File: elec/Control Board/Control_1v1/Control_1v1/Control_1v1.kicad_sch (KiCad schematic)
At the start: 69 parts, among them J1 DB9_Female_MountingHoles, J10 Conn_02x12_Odd_Even, J11 Screw_Terminal_01x02, J14 Conn_01x10, J2 Conn_01x08, J25 Screw_Terminal_01x02, J3 Conn_01x08, J4 Conn_01x08, J5 Conn_01x08, J6 Conn_01x08, J7 Conn_01x10, J8 Conn_02x18_Odd_Even, J9 Conn_01x10

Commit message: Add sheet with title block.
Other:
- moved on the sheet: A1, C104, C301, H1, H2, H3, H4, H5, ISO1, ISO2, ISO3, ISO4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

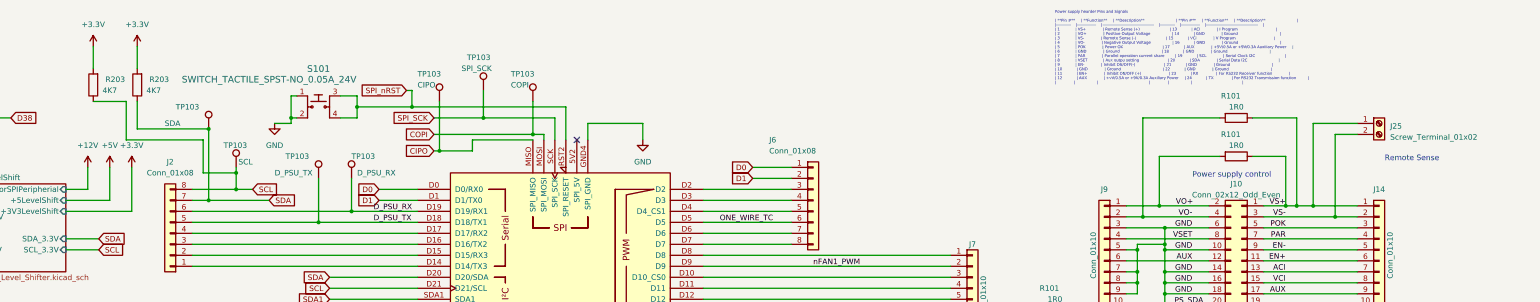
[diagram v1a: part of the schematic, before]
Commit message: Fix J10 backwards.
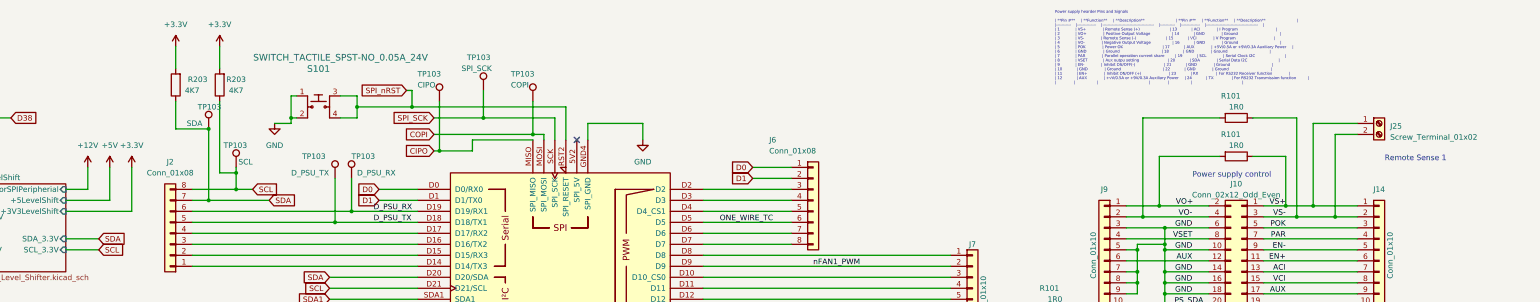
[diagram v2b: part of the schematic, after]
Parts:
- J10: footprint Connector_PinHeader_2.00mm:PinHeader_2x12_P2.00mm_Vertical -> PubInv_KiCad_PCB.pretty:PinHeader_2x12_P2.00mm_Vertical_JST
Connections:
- net VS+: no longer R101.1
- net VS-: now also R101.1
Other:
- note added: "Remote Sense 1"
- note removed: "Remote Sense"
- title: Control Interconnect Board -> Control Interconnect Board OEDCS
- moved on the sheet: R203, TP103

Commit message: Add second power supply connector. Add second and third SSR Driver. Add reset discharge.
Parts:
- removed J11: Screw_Terminal_01x02, TerminalBlock_TE-Connectivity:TerminalBlock_TE_282834-2_1x02_P2.54mm_Horizontal, symbol Connector:Screw_Terminal_01x02
- added C301: 39pF, Capacitor_SMD:C_0603_1608Metric_Pad1.08x0.95mm_HandSolder, symbol Device:C
- added D?: 1N5819WS, Diode_SMD:D_SOD-323, symbol Diode:1N5819WS
- added J? (x2): Conn_01x10, Connector_PinSocket_2.54mm:PinSocket_1x10_P2.54mm_Vertical, symbol Connector_Generic:Conn_01x10
- added J?: Conn_02x12_Odd_Even, PubInv_KiCad_PCB.pretty:PinHeader_2x12_P2.00mm_Vertical_JST, symbol Connector_Generic:Conn_02x12_Odd_Even
- added J?: Screw_Terminal_01x02, TerminalBlock_TE-Connectivity:TerminalBlock_TE_282834-2_1x02_P2.54mm_Horizontal, symbol Connector:Screw_Terminal_01x02
- added R101 (x10): 1R0, Resistor_SMD:R_0603_1608Metric_Pad0.98x0.95mm_HandSolder, symbol Device:R
- added R102 (x7): 10K, Resistor_SMD:R_0603_1608Metric_Pad0.98x0.95mm_HandSolder, symbol Device:R
- added R203: 4K7, Resistor_SMD:R_0603_1608Metric_Pad0.98x0.95mm_HandSolder, symbol Device:R
- added R301 (x2): 1R, Resistor_SMD:R_0603_1608Metric_Pad0.98x0.95mm_HandSolder, symbol Device:R
- added TP103: +24V, TestPoint:TestPoint_Loop_D2.54mm_Drill1.5mm_Beaded, symbol Connector:TestPoint
- added TP103: D_PSU_RX2, TestPoint:TestPoint_Loop_D2.54mm_Drill1.5mm_Beaded, symbol Connector:TestPoint
- added TP103: D_PSU_TX2, TestPoint:TestPoint_Loop_D2.54mm_Drill1.5mm_Beaded, symbol Connector:TestPoint
- added TP103: +12V, TestPoint:TestPoint_Loop_D2.54mm_Drill1.5mm_Beaded, symbol Connector:TestPoint
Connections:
- net +12V: now also TP103.1
- net +24V: now also R102.2, R102.2, TP103.1
- net +3.3V: now also D?.1 (K)
- net ACI: now also J?.13 (Pin_13), J?.7 (Pin_7)
- net AUX: now also J?.10 (Pin_10), J?.12 (Pin_12), J?.17 (Pin_17), J?.21 (Pin_21), J?.6 (Pin_6), J?.9 (Pin_9)
- net CIPO: now also R101.2
- net COPI: now also R101.2
- net D32: now also R101.2
- net D52: now also R301.1
- net D53: now also R301.1
- net D_PSU_RX: now also R101.2; no longer R101.2
- net D_PSU_TX: now also R101.1; no longer R101.1
- net EN+: now also J?.11 (Pin_11), J?.6 (Pin_6)
- net EN-: now also J?.5 (Pin_5), J?.9 (Pin_9)
- net GND: now also C301.2, J?.10 (Pin_10), J?.14 (Pin_14), J?.16 (Pin_16), J?.18 (Pin_18), J?.22 (Pin_22), J?.3 (Pin_3), J?.5 (Pin_5), J?.6 (Pin_6), J?.7 (Pin_7), J?.8 (Pin_8), J?.9 (Pin_9), R102.2, R203.1
- net PAR: now also J?.4 (Pin_4), J?.7 (Pin_7)
- net POK: now also J?.3 (Pin_3), J?.5 (Pin_5)
- net PS_SCL: now also J?.19 (Pin_19), R101.2
- net PS_SDA: now also J?.10 (Pin_10), J?.20 (Pin_20), R101.1
- net RX: now also J?.23 (Pin_23), R101.2
- net SCL: now also R101.1
- net SDA: now also R101.2
- net SPI_SCK: now also R101.2
- net SPI_nRST: now also C301.1, D?.2 (A)
- net TX: now also J?.24 (Pin_24), R101.1
- net VCI: now also J?.15 (Pin_15), J?.8 (Pin_8)
- net VO+: now also J?.1 (Pin_1), J?.2 (Pin_2), R101.2
- net VO-: now also J?.2 (Pin_2), J?.4 (Pin_4), R101.2
- net VS+: now also J?.1 (Pin_1), J?.1 (Pin_1), J?.1 (Pin_1), R101.1
- net VS-: now also J?.2 (Pin_2), J?.2 (Pin_2), J?.3 (Pin_3), R101.1
- net VSET: now also J?.4 (Pin_4), J?.8 (Pin_8)
- net SENSE_24V: now reaches A1.A1, J5.2 (Pin_2)
- net SENSE_24V: now also R102.2, R203.2
- net SENSE_12V: now reaches A1.A2, J5.3 (Pin_3)
- net SENSE_12V: now also R102.1, R102.2
- net D_PSU_TX2: now reaches A1.D16 (D16/TX2), J2.3 (Pin_3)
- net D_PSU_TX2: now also R101.1, TP103.1
- net D_PSU_RX2: now reaches A1.D17 (D17/RX2), J2.4 (Pin_4)
- net D_PSU_RX2: now also R101.2, TP103.1
- net SSR Interface/Heater renamed SSR Interface/Heater1
- new net: R102.1, R102.1 (x2)
- new net: R102.1, R102.2 (x2)
- new net SPI_ControllerLevel_Shifter/CIPO_3V3: R101.1
- new net SPI_ControllerLevel_Shifter/COPI_3V3: R101.1
- new net SPI_ControllerLevel_Shifter/COPI_nCS: R101.1
- new net SPI_ControllerLevel_Shifter/SCK_3V3: R101.1
- new net SSR Interface/Heater2: R301.2
- new net SSR Interface/Heater3: R301.2
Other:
- sheet SSR Interface ports: added Heater1, Heater2, Heater3; removed Heater, Heater_SSR_High, Heater_SSR_Low
- note added: "Power supply control 1"
- note added: "Power supply control 2"
- note added: "Remote Sense 2"
- note added: "Reset fast discharge"
- note removed: "Power supply control"
- note removed: "To SSR control."
- moved on the sheet: C104, ISO1, ISO2, ISO3, ISO4, ISO5, J10, J11, J14, J25, J9, MF1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

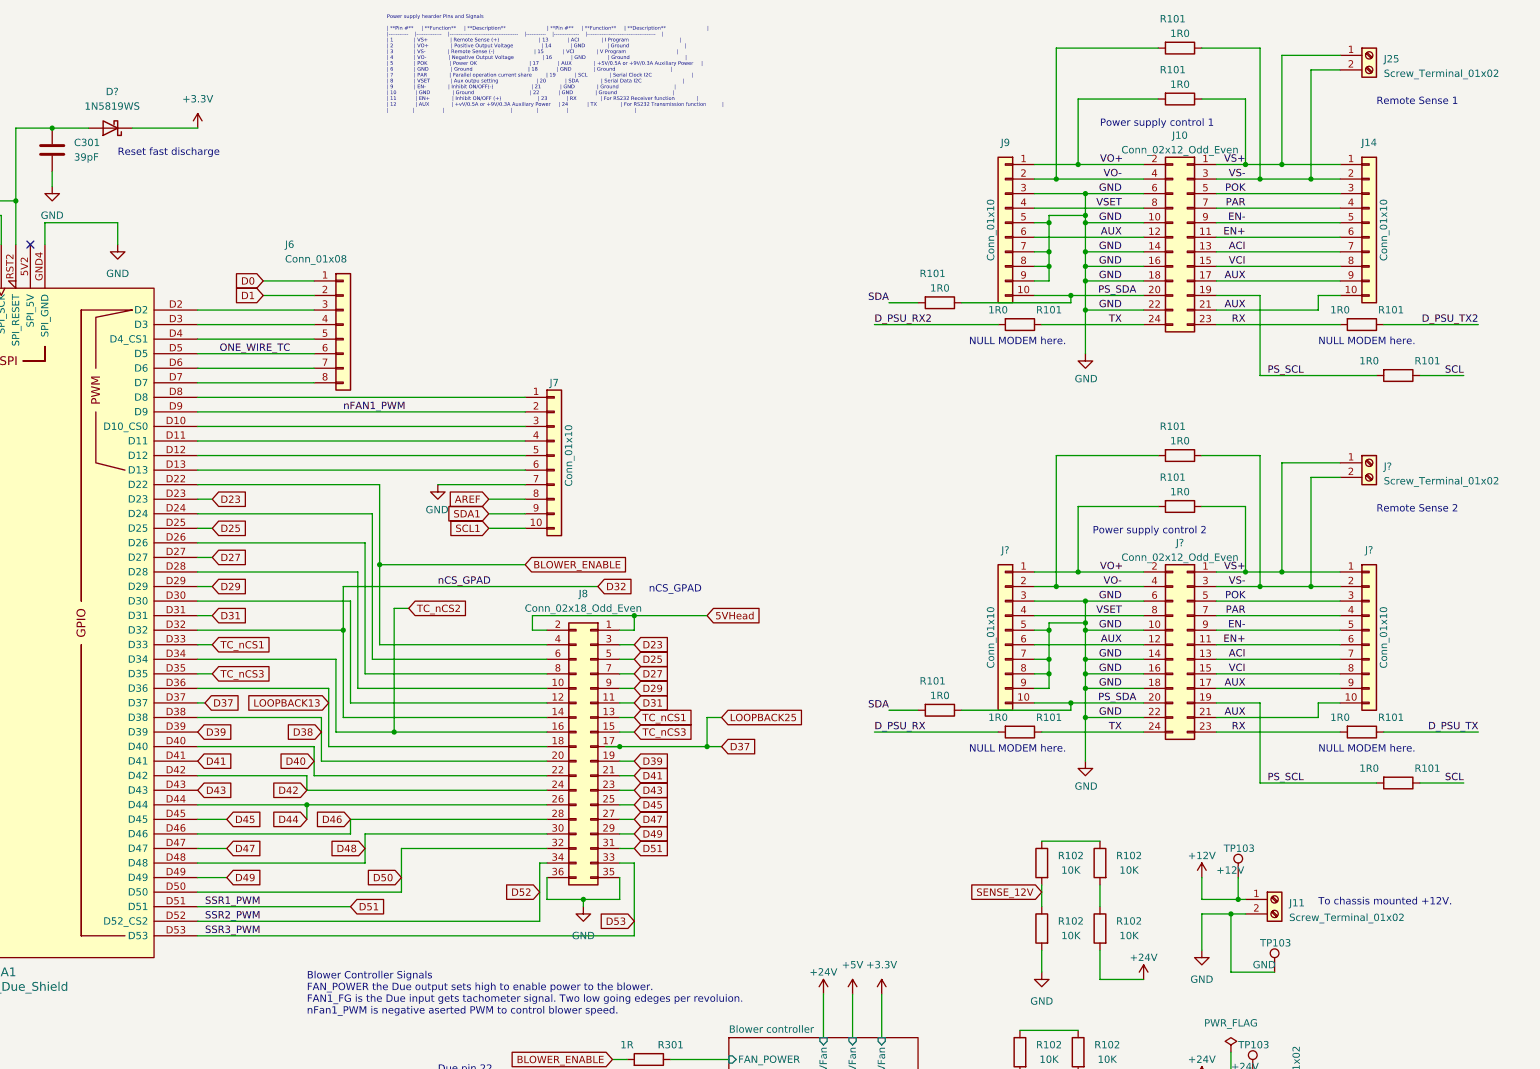
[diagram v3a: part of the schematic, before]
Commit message: Place many of new components. Still need to place SSR parts.
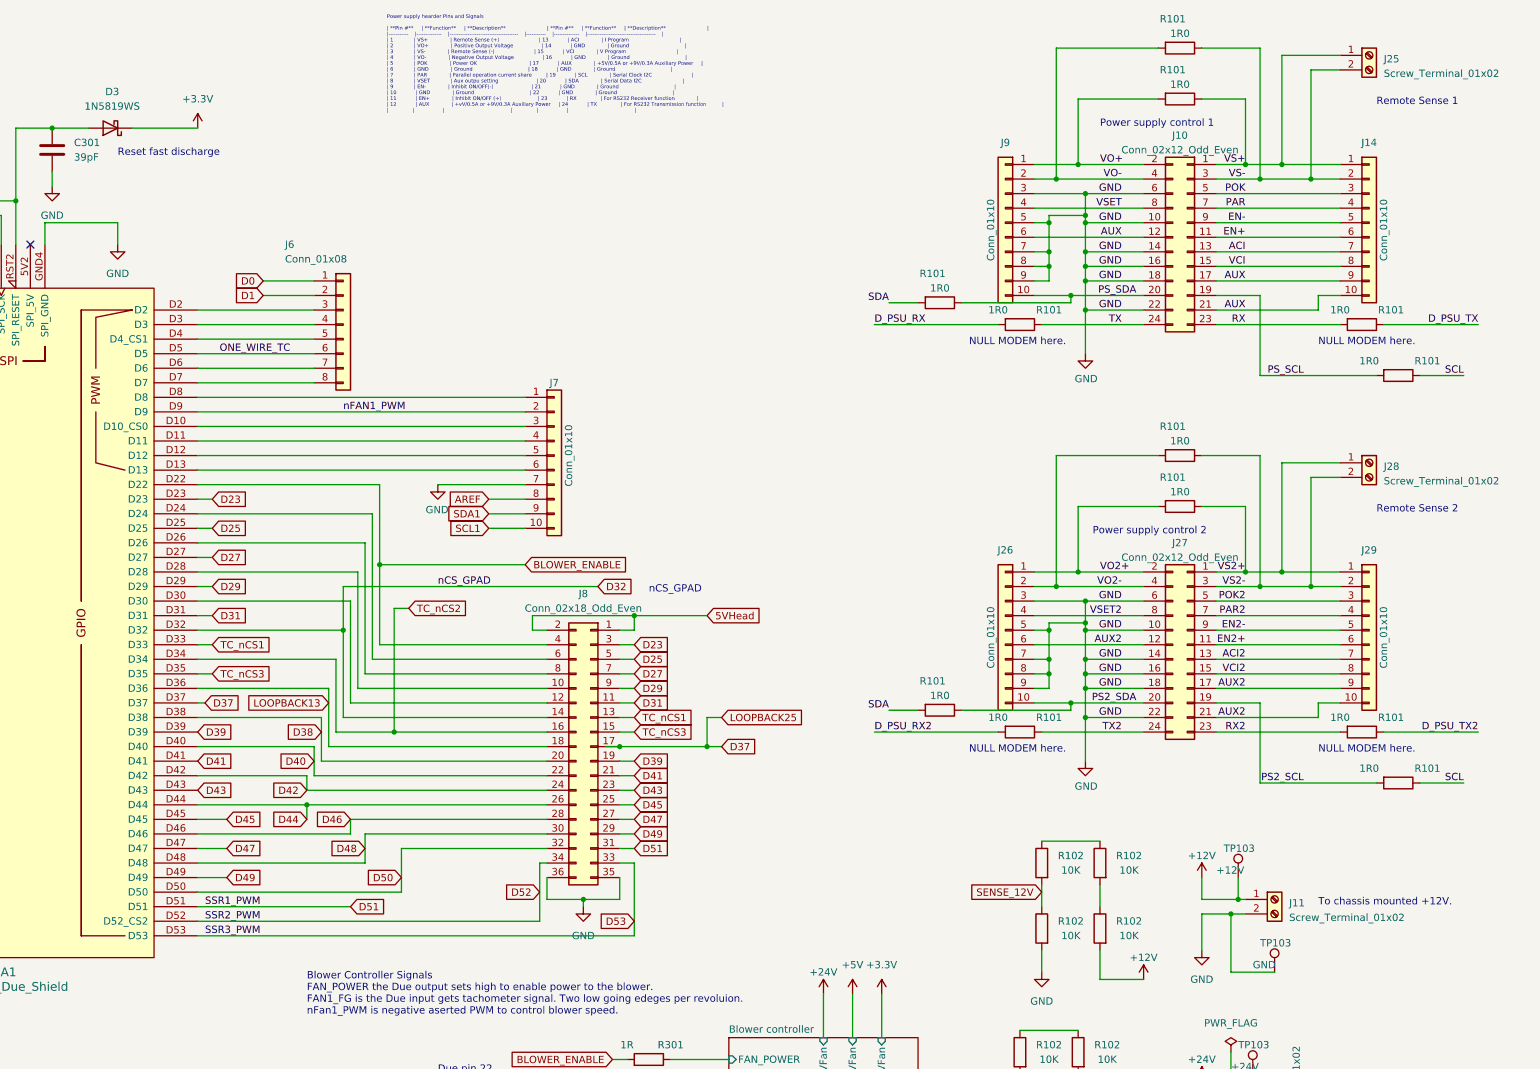
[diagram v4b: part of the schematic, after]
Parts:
- D3: renamed from D?; AssemblyType (none) -> SMT; Cost (none) -> 0.0119; Distributor 1 (none) -> JLCPCB; Distributor 1 PN (none) -> C191023; MPN (none) -> 1N5819WS; Manufacturer (none) -> Guangdong Hottech
- gave numbers to parts that had none: 4
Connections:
- net +12V: now also R102.2
- net +24V: no longer R102.2
- net ACI: no longer J27.13 (Pin_13), J29.7 (Pin_7)
- net AUX: no longer J26.6 (Pin_6), J27.12 (Pin_12), J27.17 (Pin_17), J27.21 (Pin_21), J29.10 (Pin_10), J29.9 (Pin_9)
- net D_PSU_RX: now also R101.2; no longer R101.2
- net D_PSU_RX2: now also R101.2; no longer R101.2
- net D_PSU_TX: now also R101.1; no longer R101.1
- net D_PSU_TX2: now also R101.1; no longer R101.1
- net EN+: no longer J27.11 (Pin_11), J29.6 (Pin_6)
- net EN-: no longer J27.9 (Pin_9), J29.5 (Pin_5)
- net PAR: no longer J27.7 (Pin_7), J29.4 (Pin_4)
- net POK: no longer J27.5 (Pin_5), J29.3 (Pin_3)
- net PS_SCL: no longer J27.19 (Pin_19), R101.2
- net PS_SDA: no longer J26.10 (Pin_10), J27.20 (Pin_20), R101.1
- net RX: no longer J27.23 (Pin_23), R101.2
- net TX: no longer J27.24 (Pin_24), R101.1
- net VCI: no longer J27.15 (Pin_15), J29.8 (Pin_8)
- net VO+: no longer J26.1 (Pin_1), J27.2 (Pin_2), R101.2
- net VO-: no longer J26.2 (Pin_2), J27.4 (Pin_4), R101.2
- net VS+: no longer J27.1 (Pin_1), J28.1 (Pin_1), J29.1 (Pin_1), R101.1
- net VS-: no longer J27.3 (Pin_3), J28.2 (Pin_2), J29.2 (Pin_2), R101.1
- net VSET: no longer J26.4 (Pin_4), J27.8 (Pin_8)
- new net ACI2: J27.13 (Pin_13), J29.7 (Pin_7)
- new net AUX2: J26.6 (Pin_6), J27.12 (Pin_12), J27.17 (Pin_17), J27.21 (Pin_21), J29.10 (Pin_10), J29.9 (Pin_9)
- new net EN2+: J27.11 (Pin_11), J29.6 (Pin_6)
- new net EN2-: J27.9 (Pin_9), J29.5 (Pin_5)
- new net PAR2: J27.7 (Pin_7), J29.4 (Pin_4)
- new net POK2: J27.5 (Pin_5), J29.3 (Pin_3)
- new net PS2_SCL: J27.19 (Pin_19), R101.2
- new net PS2_SDA: J26.10 (Pin_10), J27.20 (Pin_20), R101.1
- new net RX2: J27.23 (Pin_23), R101.2
- new net TX2: J27.24 (Pin_24), R101.1
- new net VCI2: J27.15 (Pin_15), J29.8 (Pin_8)
- new net VO2+: J26.1 (Pin_1), J27.2 (Pin_2), R101.2
- new net VO2-: J26.2 (Pin_2), J27.4 (Pin_4), R101.2
- new net VS2+: J27.1 (Pin_1), J28.1 (Pin_1), J29.1 (Pin_1), R101.1
- new net VS2-: J27.3 (Pin_3), J28.2 (Pin_2), J29.2 (Pin_2), R101.1
- new net VSET2: J26.4 (Pin_4), J27.8 (Pin_8)

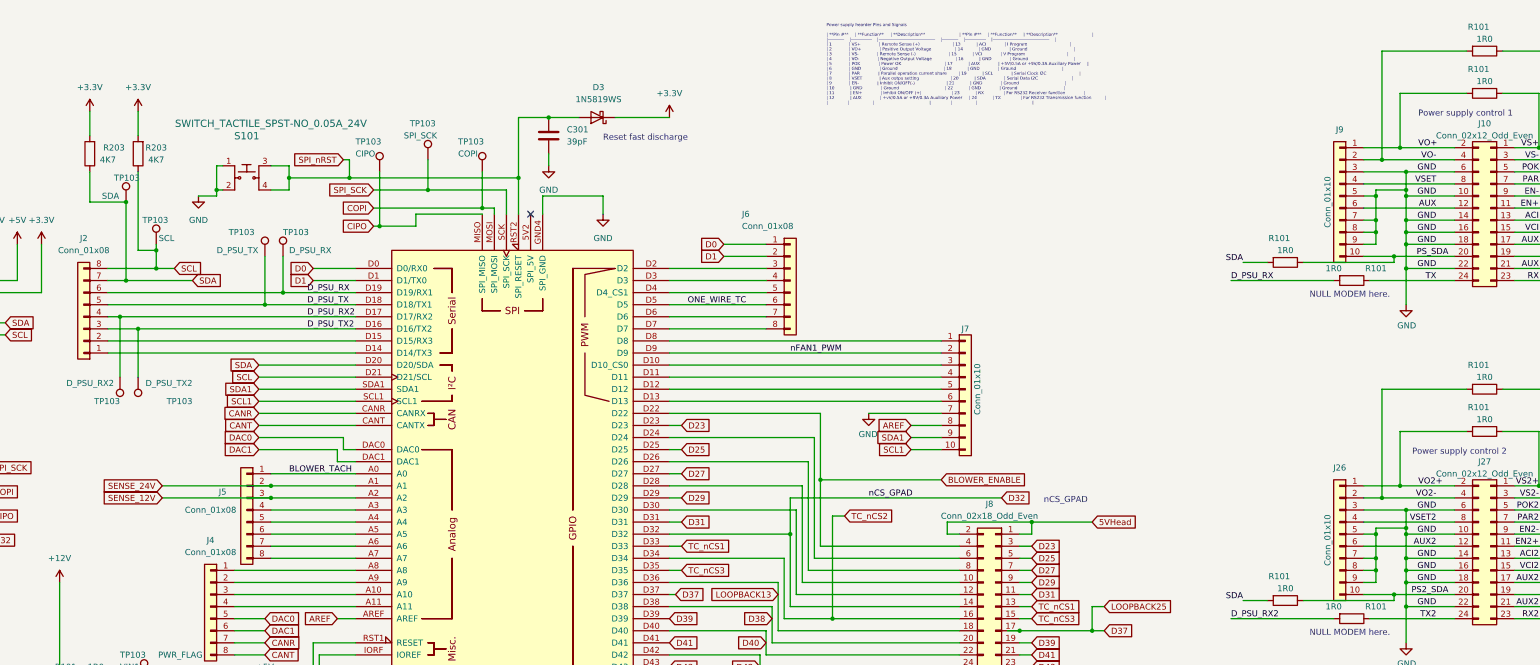
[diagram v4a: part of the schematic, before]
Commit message: Route AUX power sensors.
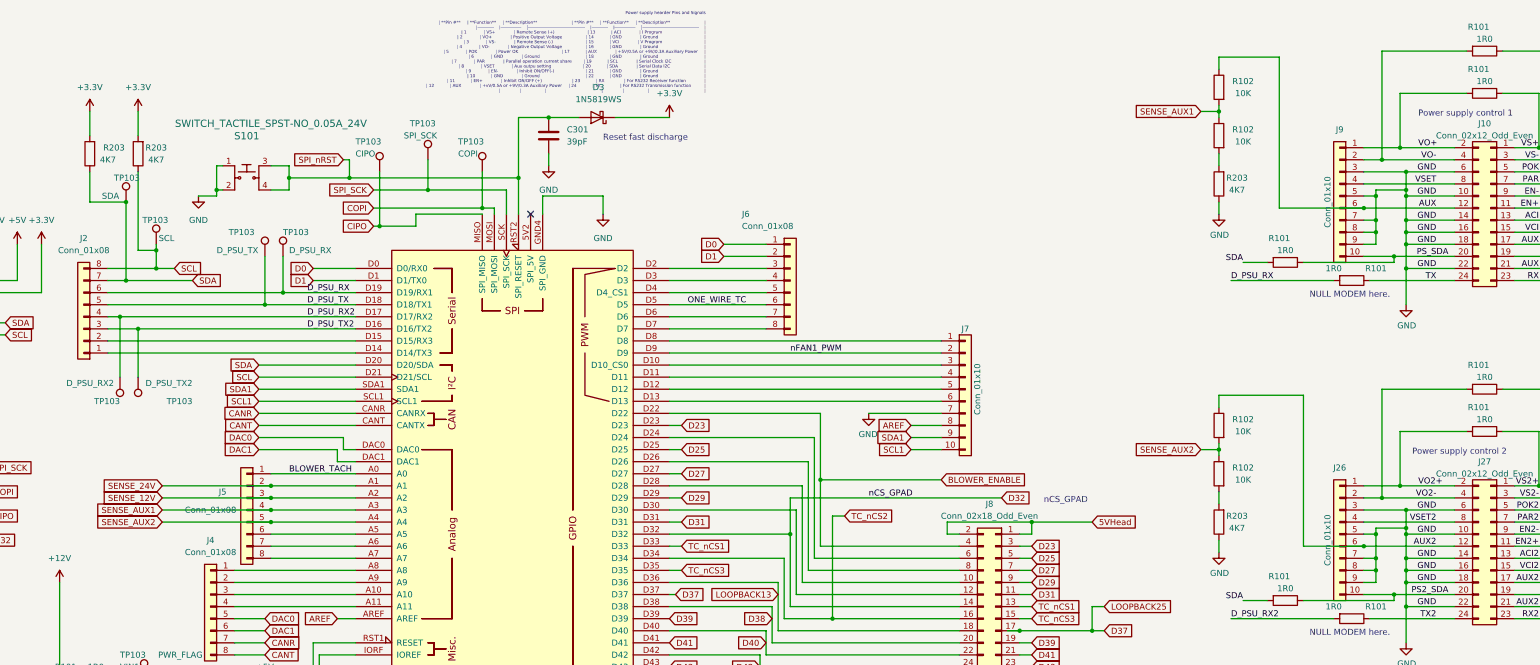
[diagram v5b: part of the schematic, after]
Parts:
- added R102 (x4): 10K, Resistor_SMD:R_0603_1608Metric_Pad0.98x0.95mm_HandSolder, symbol Device:R
- added R203 (x2): 4K7, Resistor_SMD:R_0603_1608Metric_Pad0.98x0.95mm_HandSolder, symbol Device:R
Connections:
- net AUX: now also R102.1
- net AUX2: now also R102.1
- net GND: now also R203.1, R203.1
- net SENSE_AUX1: now reaches A1.A3, J5.4 (Pin_4)
- net SENSE_AUX1: now also R102.1, R102.2
- net SENSE_AUX2: now reaches A1.A4, J5.5 (Pin_5)
- net SENSE_AUX2: now also R102.1, R102.2
- new net: R102.2, R203.2 (x2)
